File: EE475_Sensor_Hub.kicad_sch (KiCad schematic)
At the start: 5 parts, among them J1 Conn_01x04_Female, J2 Conn_01x04_Female, J3 Conn_01x15_Female, J4 Conn_01x15_Female

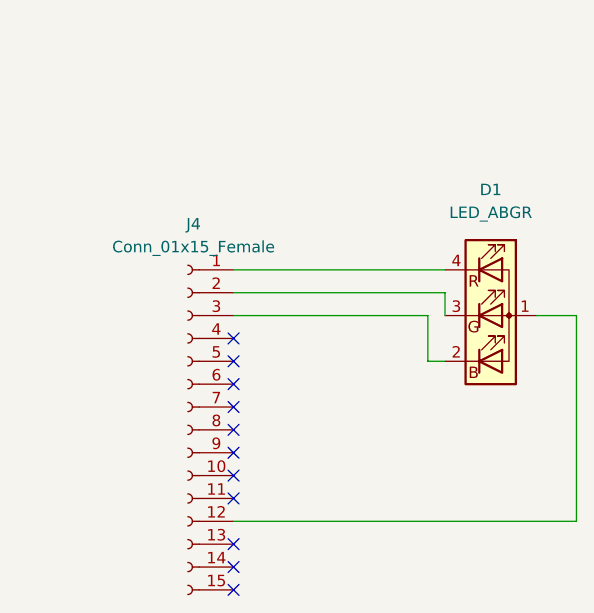
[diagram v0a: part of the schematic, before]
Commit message: Updated version of the PCB based on professor and TAs feedback
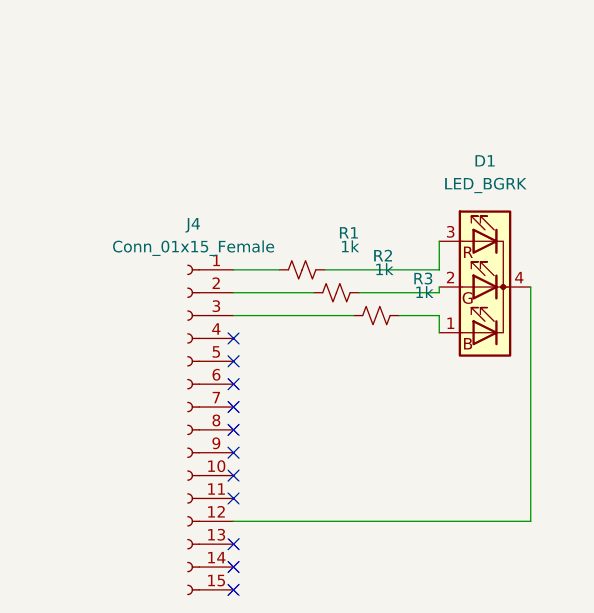
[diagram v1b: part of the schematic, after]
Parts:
- removed D1: LED_ABGR, LED_SMD:LED_RGB_1210, symbol Device:LED_ABGR
- added D1: LED_BGRK, LED_SMD:LED_RGB_1210, symbol Device:LED_BGRK
- added R1, R2, R3: 1k, Resistor_SMD:R_0402_1005Metric, symbol Device:R_Small_US
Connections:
- net at J4.12 (Pin_12): now also D1.4 (K)
- net at J4.3 (Pin_3): now also R3.1
- net at J4.2 (Pin_2): now also R2.1
- net at J4.1 (Pin_1): now also R1.1
- new net: D1.2 (GA), R2.2
- new net: D1.1 (BA), R3.2
- new net: D1.3 (RA), R1.2
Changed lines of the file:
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@@
   (no_connect (at 180.34 113.03))
   (no_connect (at 180.34 115.57))
+  (wire (pts (xy 203.2 100.33) (xy 203.2 102.235))
+    (stroke (width 0) (type default) (color 0 0 0 0))
+  )
   (wire (pts (xy 120.015 81.28) (xy 128.27 81.28))
     (stroke (width 0) (type default) (color 0 0 0 0))
@@
     (stroke (width 0) (type default) (color 0 0 0 0))
   )
-  (wire (pts (xy 218.44 100.33) (xy 218.44 123.19))
-    (stroke (width 0) (type default) (color 0 0 0 0))
-  )
-  (wire (pts (xy 201.93 100.33) (xy 201.93 105.41))
-    (stroke (width 0) (type default) (color 0 0 0 0))
-  )
-  (wire (pts (xy 180.34 97.79) (xy 203.835 97.79))
+  (wire (pts (xy 203.2 95.25) (xy 203.2 92.075))
+    (stroke (width 0) (type default) (color 0 0 0 0))
+  )
+  (wire (pts (xy 203.2 97.79) (xy 203.2 97.155))
+    (stroke (width 0) (type default) (color 0 0 0 0))
+  )
+  (wire (pts (xy 198.755 100.33) (xy 203.2 100.33))
     (stroke (width 0) (type default) (color 0 0 0 0))
   )
@@
     (stroke (width 0) (type default) (color 0 0 0 0))
   )
-  (wire (pts (xy 201.93 105.41) (xy 203.835 105.41))
-    (stroke (width 0) (type default) (color 0 0 0 0))
-  )
-  (wire (pts (xy 180.34 95.25) (xy 203.835 95.25))
+  (wire (pts (xy 213.36 123.19) (xy 180.34 123.19))
+    (stroke (width 0) (type default) (color 0 0 0 0))
+  )
+  (wire (pts (xy 180.34 97.79) (xy 189.23 97.79))
     (stroke (width 0) (type default) (color 0 0 0 0))
   )
@@
     (stroke (width 0) (type default) (color 0 0 0 0))
   )
-  (wire (pts (xy 180.34 100.33) (xy 201.93 100.33))
+  (wire (pts (xy 194.31 97.79) (xy 203.2 97.79))
     (stroke (width 0) (type default) (color 0 0 0 0))
   )
@@
     (stroke (width 0) (type default) (color 0 0 0 0))
   )
-  (wire (pts (xy 213.995 100.33) (xy 218.44 100.33))
+  (wire (pts (xy 180.34 100.33) (xy 193.675 100.33))
     (stroke (width 0) (type default) (color 0 0 0 0))
   )
@@
     (stroke (width 0) (type default) (color 0 0 0 0))
   )
-  (wire (pts (xy 218.44 123.19) (xy 180.34 123.19))
-    (stroke (width 0) (type default) (color 0 0 0 0))
-  )
-  (wire (pts (xy 203.835 97.79) (xy 203.835 100.33))
+  (wire (pts (xy 213.36 97.155) (xy 213.36 123.19))
+    (stroke (width 0) (type default) (color 0 0 0 0))
+  )
+  (wire (pts (xy 180.34 95.25) (xy 185.42 95.25))
+    (stroke (width 0) (type default) (color 0 0 0 0))
+  )
+  (wire (pts (xy 190.5 95.25) (xy 203.2 95.25))
     (stroke (width 0) (type default) (color 0 0 0 0))
   )
@@
     (pin "9")
   )
-  (symbol (lib_id "Device:LED_ABGR") (at 208.915 100.33 0) (unit 1)
-    (in_bom yes) (on_board yes) (fields_autoplaced)
-    (property "Reference" "D1" (id 0) (at 208.915 86.36 0))
-    (property "Value" "LED_ABGR" (id 1) (at 208.915 88.9 0))
-    (property "Footprint" "LED_SMD:LED_RGB_1210" (id 2) (at 208.915 101.6 0)
-      (effects (font (size 1.27 1.27)) hide)
-    )
-    (property "Datasheet" "~" (id 3) (at 208.915 101.6 0)
-      (effects (font (size 1.27 1.27)) hide)
-    )
-    (pin "1")
-    (pin "2")
-    (pin "3")
-    (pin "4")
+  (symbol (lib_id "Device:R_Small_US") (at 191.77 97.79 90) (unit 1)
+    (in_bom yes) (on_board yes)
+    (property "Reference" "R2" (id 0) (at 198.12 93.726 90)
+      (effects (font (size 1.27 1.27)) (justify left))
+    )
+    (property "Value" "1k" (id 1) (at 198.12 95.25 90)
+      (effects (font (size 1.27 1.27)) (justify left))
+    )
+    (property "Footprint" "Resistor_SMD:R_0402_1005Metric" (id 2) (at 191.77 97.79 0)
+      (effects (font (size 1.27 1.27)) hide)
+    )
+    (property "Datasheet" "~" (id 3) (at 191.77 97.79 0)
+      (effects (font (size 1.27 1.27)) hide)
+    )
+    (pin "1")
+    (pin "2")
   )
   (symbol (lib_id "Connector:Conn_01x04_Female") (at 133.35 76.2 0) (unit 1)
@@
     (pin "3")
     (pin "4")
+  )
+  (symbol (lib_id "Device:R_Small_US") (at 196.215 100.33 90) (unit 1)
+    (in_bom yes) (on_board yes)
+    (property "Reference" "R3" (id 0) (at 202.565 96.266 90)
+      (effects (font (size 1.27 1.27)) (justify left))
+    )
+    (property "Value" "1k" (id 1) (at 202.565 97.79 90)
+      (effects (font (size 1.27 1.27)) (justify left))
+    )
+    (property "Footprint" "Resistor_SMD:R_0402_1005Metric" (id 2) (at 196.215 100.33 0)
+      (effects (font (size 1.27 1.27)) hide)
+    )
+    (property "Datasheet" "~" (id 3) (at 196.215 100.33 0)
+      (effects (font (size 1.27 1.27)) hide)
+    )
+    (pin "1")
+    (pin "2")
   )
   (symbol (lib_id "Connector:Conn_01x15_Female") (at 175.26 113.03 0) (mirror y) (unit 1)
@@
     (pin "4")
   )
+  (symbol (lib_id "Device:LED_BGRK") (at 208.28 97.155 0) (mirror y) (unit 1)
+    (in_bom yes) (on_board yes) (fields_autoplaced)
+    (property "Reference" "D1" (id 0) (at 208.28 83.185 0))
+    (property "Value" "LED_BGRK" (id 1) (at 208.28 85.725 0))
+    (property "Footprint" "LED_SMD:LED_RGB_1210" (id 2) (at 208.28 98.425 0)
+      (effects (font (size 1.27 1.27)) hide)
+    )
+    (property "Datasheet" "~" (id 3) (at 208.28 98.425 0)
+      (effects (font (size 1.27 1.27)) hide)
+    )
+    (pin "1")
+    (pin "2")
+    (pin "3")
+    (pin "4")
+  )
+  (symbol (lib_id "Device:R_Small_US") (at 187.96 95.25 90) (unit 1)
+    (in_bom yes) (on_board yes)
+    (property "Reference" "R1" (id 0) (at 194.31 91.186 90)
+      (effects (font (size 1.27 1.27)) (justify left))
+    )
+    (property "Value" "1k" (id 1) (at 194.31 92.71 90)
+      (effects (font (size 1.27 1.27)) (justify left))
+    )
+    (property "Footprint" "Resistor_SMD:R_0402_1005Metric" (id 2) (at 187.96 95.25 0)
+      (effects (font (size 1.27 1.27)) hide)
+    )
+    (property "Datasheet" "~" (id 3) (at 187.96 95.25 0)
+      (effects (font (size 1.27 1.27)) hide)
+    )
+    (pin "1")
+    (pin "2")
+  )
   (sheet_instances
     (path "/" (page "1"))
   )
   (symbol_instances
-    (path "/3b46a986-fc4b-433b-a888-7fb3309174a6"
-      (reference "D1") (unit 1) (value "LED_ABGR") (footprint "LED_SMD:LED_RGB_1210")
+    (path "/9d3407c3-2296-4416-aebe-edd47e947609"
+      (reference "D1") (unit 1) (value "LED_BGRK") (footprint "LED_SMD:LED_RGB_1210")
     )
     (path "/89619c63-f3f9-44e2-90b3-b88ad71991b9"
@@
       (reference "J4") (unit 1) (value "Conn_01x15_Female") (footprint "Connector_PinSocket_2.54mm:PinSocket_1x15_P2.54mm_Vertical")
     )
-  )
+    (path "/f0a96fc6-4853-4e99-b3e0-30aae5fe8d40"
+      (reference "R1") (unit 1) (value "1k") (footprint "Resistor_SMD:R_0402_1005Metric")
+    )
+    (path "/501e19e5-72c5-4ce4-a545-8ee86290058d"
+      (reference "R2") (unit 1) (value "1k") (footprint "Resistor_SMD:R_0402_1005Metric")
+    )
+    (path "/63863588-8856-4c85-9394-4187a981f7c3"
+      (reference "R3") (unit 1) (value "1k") (footprint "Resistor_SMD:R_0402_1005Metric")
+    )
+  )

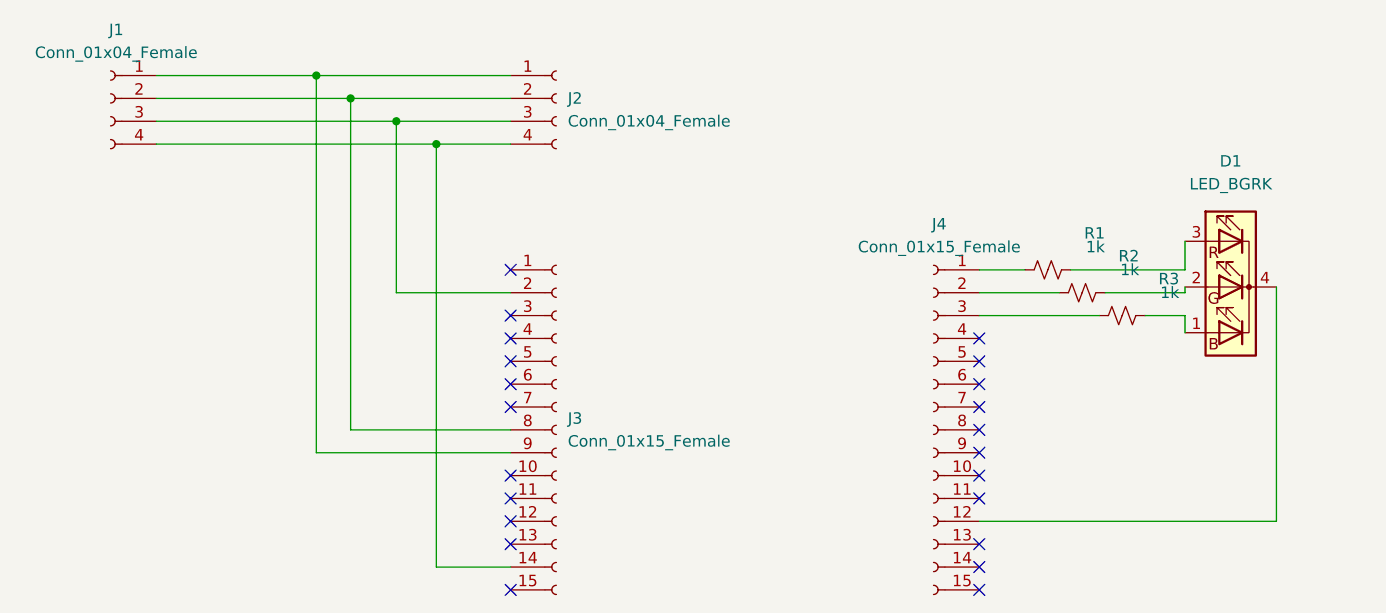
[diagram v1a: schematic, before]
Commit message: Modify LED and resistor footprint
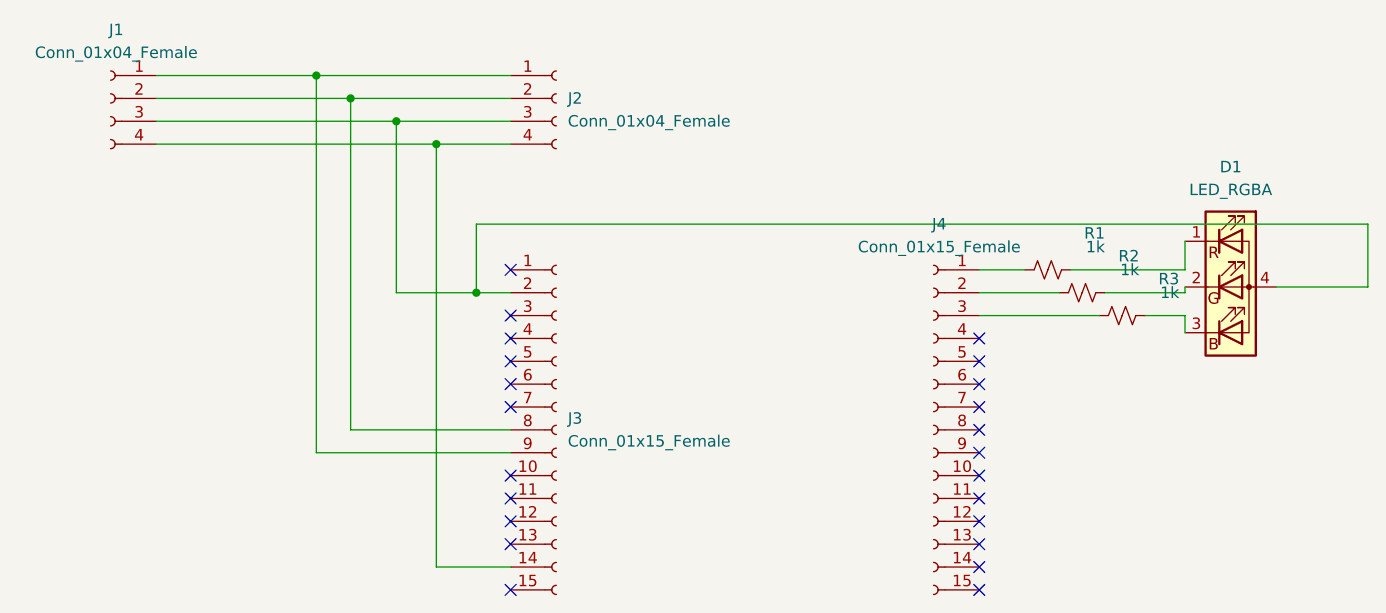
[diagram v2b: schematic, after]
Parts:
- removed D1: LED_BGRK, LED_SMD:LED_RGB_1210, symbol Device:LED_BGRK
- added D1: LED_RGBA, LED_SMD:LED_RGB_1210, symbol Device:LED_RGBA
- R1, R2, R3: footprint Resistor_SMD:R_0402_1005Metric -> Resistor_SMD:R_1206_3216Metric
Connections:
- net at J1.3 (Pin_3), J2.3 (Pin_3), J3.2 (Pin_2): now also D1.4 (A)
- net at R2.2: now also D1.2 (GK)
- net at R3.2: now also D1.3 (BK)
- net at R1.2: now also D1.1 (RK)
- no-connect marks 22 -> 23
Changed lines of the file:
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@@
   (junction (at 106.68 73.66) (diameter 0) (color 0 0 0 0)
+  )
+  (junction (at 124.46 97.79) (diameter 0) (color 0 0 0 0)
   )
   (junction (at 115.57 78.74) (diameter 0) (color 0 0 0 0)
@@
   (no_connect (at 180.34 130.81))
   (no_connect (at 128.27 100.33))
+  (no_connect (at 180.34 123.19))
   (no_connect (at 128.27 110.49))
   (no_connect (at 128.27 125.73))
@@
     (stroke (width 0) (type default) (color 0 0 0 0))
   )
+  (wire (pts (xy 124.46 97.79) (xy 128.27 97.79))
+    (stroke (width 0) (type default) (color 0 0 0 0))
+  )
   (wire (pts (xy 120.015 81.28) (xy 128.27 81.28))
     (stroke (width 0) (type default) (color 0 0 0 0))
@@
     (stroke (width 0) (type default) (color 0 0 0 0))
   )
+  (wire (pts (xy 124.46 90.17) (xy 124.46 97.79))
+    (stroke (width 0) (type default) (color 0 0 0 0))
+  )
+  (wire (pts (xy 213.36 97.155) (xy 223.52 97.155))
+    (stroke (width 0) (type default) (color 0 0 0 0))
+  )
   (wire (pts (xy 203.2 97.79) (xy 203.2 97.155))
     (stroke (width 0) (type default) (color 0 0 0 0))
@@
     (stroke (width 0) (type default) (color 0 0 0 0))
   )
-  (wire (pts (xy 213.36 123.19) (xy 180.34 123.19))
-    (stroke (width 0) (type default) (color 0 0 0 0))
-  )
   (wire (pts (xy 180.34 97.79) (xy 189.23 97.79))
     (stroke (width 0) (type default) (color 0 0 0 0))
@@
     (stroke (width 0) (type default) (color 0 0 0 0))
   )
-  (wire (pts (xy 115.57 97.79) (xy 128.27 97.79))
+  (wire (pts (xy 115.57 97.79) (xy 124.46 97.79))
     (stroke (width 0) (type default) (color 0 0 0 0))
   )
@@
     (stroke (width 0) (type default) (color 0 0 0 0))
   )
+  (wire (pts (xy 223.52 90.17) (xy 124.46 90.17))
+    (stroke (width 0) (type default) (color 0 0 0 0))
+  )
   (wire (pts (xy 88.9 73.66) (xy 106.68 73.66))
     (stroke (width 0) (type default) (color 0 0 0 0))
@@
     (stroke (width 0) (type default) (color 0 0 0 0))
   )
-  (wire (pts (xy 213.36 97.155) (xy 213.36 123.19))
-    (stroke (width 0) (type default) (color 0 0 0 0))
-  )
   (wire (pts (xy 180.34 95.25) (xy 185.42 95.25))
+    (stroke (width 0) (type default) (color 0 0 0 0))
+  )
+  (wire (pts (xy 223.52 97.155) (xy 223.52 90.17))
     (stroke (width 0) (type default) (color 0 0 0 0))
   )
@@
     (pin "9")
   )
+  (symbol (lib_id "Device:LED_RGBA") (at 208.28 97.155 0) (unit 1)
+    (in_bom yes) (on_board yes) (fields_autoplaced)
+    (property "Reference" "D1" (id 0) (at 208.28 83.82 0))
+    (property "Value" "LED_RGBA" (id 1) (at 208.28 86.36 0))
+    (property "Footprint" "LED_SMD:LED_RGB_1210" (id 2) (at 208.28 98.425 0)
+      (effects (font (size 1.27 1.27)) hide)
+    )
+    (property "Datasheet" "~" (id 3) (at 208.28 98.425 0)
+      (effects (font (size 1.27 1.27)) hide)
+    )
+    (pin "1")
+    (pin "2")
+    (pin "3")
+    (pin "4")
+  )
   (symbol (lib_id "Device:R_Small_US") (at 191.77 97.79 90) (unit 1)
     (in_bom yes) (on_board yes)
@@
       (effects (font (size 1.27 1.27)) (justify left))
     )
-    (property "Footprint" "Resistor_SMD:R_0402_1005Metric" (id 2) (at 191.77 97.79 0)
+    (property "Footprint" "Resistor_SMD:R_1206_3216Metric" (id 2) (at 191.77 97.79 0)
       (effects (font (size 1.27 1.27)) hide)
     )
@@
       (effects (font (size 1.27 1.27)) (justify left))
     )
-    (property "Footprint" "Resistor_SMD:R_0402_1005Metric" (id 2) (at 196.215 100.33 0)
+    (property "Footprint" "Resistor_SMD:R_1206_3216Metric" (id 2) (at 196.215 100.33 0)
       (effects (font (size 1.27 1.27)) hide)
     )
@@
     (pin "4")
   )
-  (symbol (lib_id "Device:LED_BGRK") (at 208.28 97.155 0) (mirror y) (unit 1)
-    (in_bom yes) (on_board yes) (fields_autoplaced)
-    (property "Reference" "D1" (id 0) (at 208.28 83.185 0))
-    (property "Value" "LED_BGRK" (id 1) (at 208.28 85.725 0))
-    (property "Footprint" "LED_SMD:LED_RGB_1210" (id 2) (at 208.28 98.425 0)
-      (effects (font (size 1.27 1.27)) hide)
-    )
-    (property "Datasheet" "~" (id 3) (at 208.28 98.425 0)
-      (effects (font (size 1.27 1.27)) hide)
-    )
-    (pin "1")
-    (pin "2")
-    (pin "3")
-    (pin "4")
-  )
   (symbol (lib_id "Device:R_Small_US") (at 187.96 95.25 90) (unit 1)
     (in_bom yes) (on_board yes)
@@
       (effects (font (size 1.27 1.27)) (justify left))
     )
-    (property "Footprint" "Resistor_SMD:R_0402_1005Metric" (id 2) (at 187.96 95.25 0)
+    (property "Footprint" "Resistor_SMD:R_1206_3216Metric" (id 2) (at 187.96 95.25 0)
       (effects (font (size 1.27 1.27)) hide)
     )
@@
   )
   (symbol_instances
-    (path "/9d3407c3-2296-4416-aebe-edd47e947609"
-      (reference "D1") (unit 1) (value "LED_BGRK") (footprint "LED_SMD:LED_RGB_1210")
+    (path "/3c6a00c7-6216-4a35-b701-41846b3f48e7"
+      (reference "D1") (unit 1) (value "LED_RGBA") (footprint "LED_SMD:LED_RGB_1210")
     )
     (path "/89619c63-f3f9-44e2-90b3-b88ad71991b9"
@@
     )
     (path "/f0a96fc6-4853-4e99-b3e0-30aae5fe8d40"
-      (reference "R1") (unit 1) (value "1k") (footprint "Resistor_SMD:R_0402_1005Metric")
+      (reference "R1") (unit 1) (value "1k") (footprint "Resistor_SMD:R_1206_3216Metric")
     )
     (path "/501e19e5-72c5-4ce4-a545-8ee86290058d"
-      (reference "R2") (unit 1) (value "1k") (footprint "Resistor_SMD:R_0402_1005Metric")
+      (reference "R2") (unit 1) (value "1k") (footprint "Resistor_SMD:R_1206_3216Metric")
     )
     (path "/63863588-8856-4c85-9394-4187a981f7c3"
-      (reference "R3") (unit 1) (value "1k") (footprint "Resistor_SMD:R_0402_1005Metric")
-    )
-  )
+      (reference "R3") (unit 1) (value "1k") (footprint "Resistor_SMD:R_1206_3216Metric")
+    )
+  )
